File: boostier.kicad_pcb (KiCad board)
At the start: 2 copper layers, 7 parts, among them U1 TLV61070ADBV, U2 SN74LV1T126DBVR

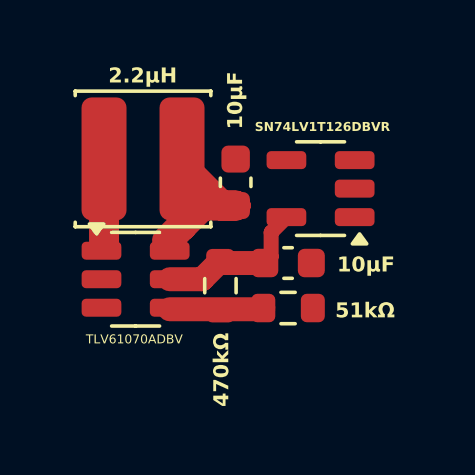
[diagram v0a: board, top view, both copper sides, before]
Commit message: Cleanup schematic/PCB mismatching net names
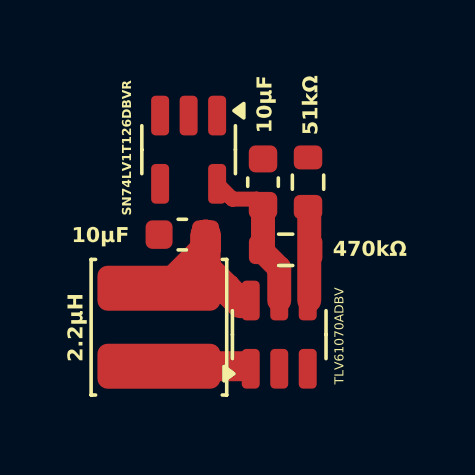
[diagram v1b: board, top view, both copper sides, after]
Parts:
- moved L1 5.63 mm to (158.9, 100.3), turned to -90 degrees
- moved U1 5.13 mm to (162.9, 100.5), turned to 90 degrees
- moved U2 4.58 mm to (159.8, 94.4), turned to -90 degrees
- moved R2 4.25 mm to (163.8, 95.4), turned to 90 degrees
- moved C2 2.82 mm to (162.3, 95.4), turned to 90 degrees
- moved C1 2.49 mm to (159.6, 97.2), turned to 180 degrees
- moved R1 2.48 mm to (163.1, 97.7), turned to 0 degrees

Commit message: Cleanup.
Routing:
- net RAW: track 7.58 -> 0.24 mm
- net 5V: track 5.28 -> 0.30 mm
- net BOOST_SW: track 2.75 -> 0.00 mm
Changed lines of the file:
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@@
-	)
-	(segment
-		(start 159.1025 98.97)
-		(end 160.415 97.6575)
-		(width 1)
-		(layer "F.Cu")
-		(net 1)
-	)
-	(segment
-		(start 158.86 98.97)
-		(end 161.09 98.97)
-		(width 1)
-		(layer "F.Cu")
-		(net 1)
-	)
-	(segment
-		(start 160.415 98.295)
-		(end 161.09 98.97)
-		(width 1)
-		(layer "F.Cu")
-		(net 1)
 	)
 	(segment
@@
 	)
 	(segment
-		(start 161.09 98.97)
-		(end 161.59 99.47)
-		(width 1)
-		(layer "F.Cu")
-		(net 1)
-	)
-	(segment
-		(start 160.415 97.6575)
-		(end 160.415 97.1825)
-		(width 1)
-		(layer "F.Cu")
-		(net 1)
-	)
-	(segment
-		(start 160.415 97.1825)
-		(end 160.415 98.295)
-		(width 1)
-		(layer "F.Cu")
-		(net 1)
-	)
-	(segment
-		(start 160.8 95.49)
-		(end 161.31 96)
-		(width 0.5)
-		(layer "F.Cu")
-		(net 3)
-	)
-	(segment
-		(start 162.33 97.62)
-		(end 162.26 97.69)
-		(width 0.8)
-		(layer "F.Cu")
-		(net 3)
-	)
-	(segment
-		(start 161.31 96)
-		(end 162.12 96)
-		(width 0.5)
-		(layer "F.Cu")
-		(net 3)
-	)
-	(segment
 		(start 162.12 96)
 		(end 162.33 96.21)
@@
 	)
 	(segment
-		(start 162.87 99.38)
-		(end 162.87 98.3)
-		(width 0.8)
+		(start 163.82 99.38)
+		(end 163.82 96.27)
+		(width 0.2)
 		(layer "F.Cu")
-		(net 3)
+		(net 7)
 	)
 	(segment
-		(start 162.33 96.21)
-		(end 162.33 97.62)
-		(width 0.8)
-		(layer "F.Cu")
-		(net 3)
-	)
-	(segment
-		(start 162.87 98.3)
-		(end 162.26 97.69)
-		(width 0.8)
-		(layer "F.Cu")
-		(net 3)
-	)
-	(segment
-		(start 163.871 96.301)
-		(end 163.871 99.38)
-		(width 0.8)
+		(start 163.82 96.27)
+		(end 163.83 96.26)
+		(width 0.2)
 		(layer "F.Cu")
 		(net 7)
@@
 		(net 7)
 	)
-	(segment
-		(start 158.86 101.57)
-		(end 161.61 101.57)
-		(width 1)
-		(layer "F.Cu")
-		(net 8)
-	)
 	(embedded_fonts no)
